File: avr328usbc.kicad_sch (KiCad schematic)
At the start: 18 parts, among them J1 USB-C THT, J2 MCP Debug Header, J3 USB-C THT, U1 MCP2221AxP, U2 ACPL-772L-000E, U3 ACPL-772L-000E

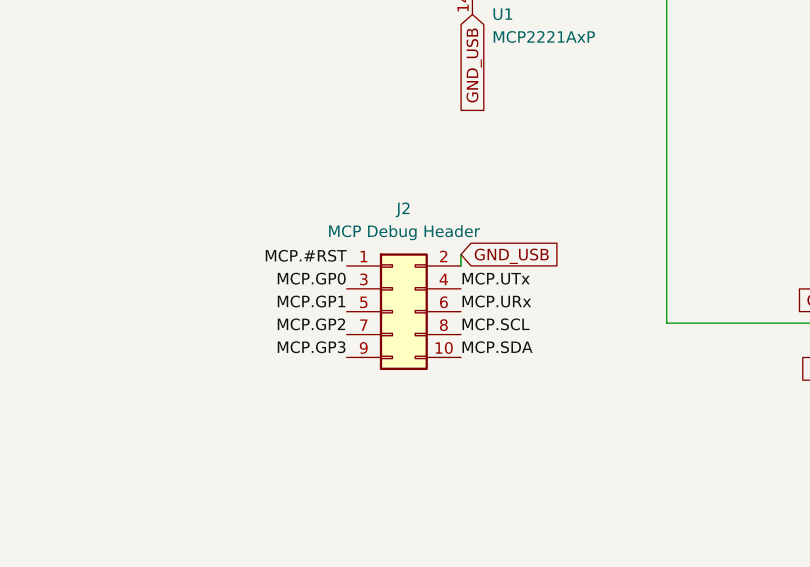
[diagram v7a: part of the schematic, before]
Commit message: reordered pins and routed MCP header
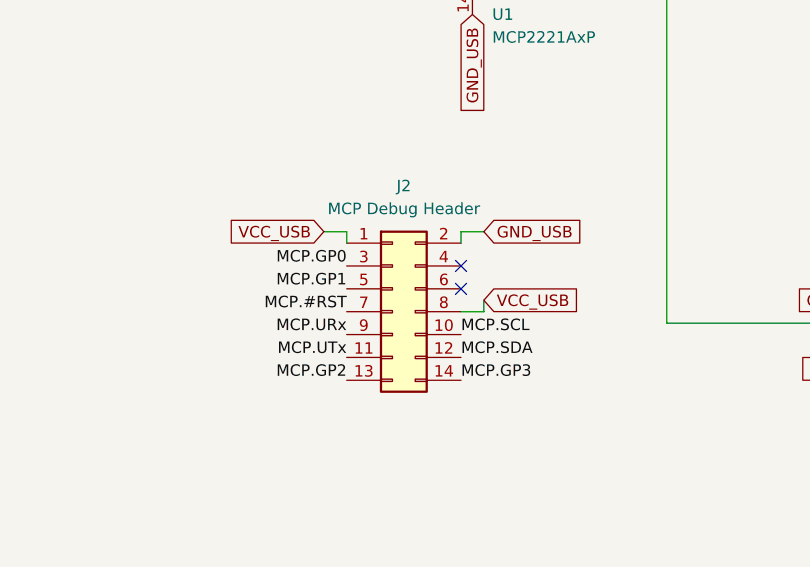
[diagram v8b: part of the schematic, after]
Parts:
- J2: footprint Connector_PinHeader_2.54mm:PinHeader_2x05_P2.54mm_Vertical -> Connector_PinHeader_2.54mm:PinHeader_2x07_P2.54mm_Vertical; symbol Connector_Generic:Conn_02x05_Odd_Even -> Connector_Generic:Conn_02x07_Odd_Even
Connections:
- net MCP.#RST: now also J2.7 (Pin_7); no longer J2.1 (Pin_1)
- net MCP.GP2: now also J2.13 (Pin_13); no longer J2.7 (Pin_7)
- net MCP.GP3: now also J2.14 (Pin_14); no longer J2.9 (Pin_9)
- net MCP.SCL: now also J2.10 (Pin_10); no longer J2.8 (Pin_8)
- net MCP.SDA: now also J2.12 (Pin_12); no longer J2.10 (Pin_10)
- net MCP.URx: now also J2.9 (Pin_9); no longer J2.6 (Pin_6)
- net MCP.UTx: now also J2.11 (Pin_11); no longer J2.4 (Pin_4)
- net VCC_USB: now also J2.1 (Pin_1), J2.8 (Pin_8)
- no-connect marks 8 -> 10
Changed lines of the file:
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@@
+	)
+	(no_connect
+		(at 104.14 118.11)
 	)
 	(no_connect
 		(at 45.72 68.58)
 	)
+	(no_connect
+		(at 104.14 120.65)
+	)
 	(wire
 		(pts
@@
 	(wire
 		(pts
+			(xy 106.68 121.92) (xy 106.68 123.19)
+		)
+		(stroke
+			(width 0)
+			(type default)
+		)
+	)
+	(wire
+		(pts
 			(xy 52.07 74.93) (xy 95.25 74.93)
 		)
@@
 	(wire
 		(pts
+			(xy 104.14 114.3) (xy 104.14 115.57)
+		)
+		(stroke
+			(width 0)
+			(type default)
+		)
+	)
+	(wire
+		(pts
 			(xy 24.13 161.29) (xy 24.13 166.37)
 		)
@@
 	(wire
 		(pts
+			(xy 88.9 114.3) (xy 91.44 114.3)
+		)
+		(stroke
+			(width 0)
+			(type default)
+		)
+	)
+	(wire
+		(pts
 			(xy 64.77 179.07) (xy 52.07 179.07)
 		)
@@
 	(wire
 		(pts
+			(xy 91.44 114.3) (xy 91.44 115.57)
+		)
+		(stroke
+			(width 0)
+			(type default)
+		)
+	)
+	(wire
+		(pts
 			(xy 121.92 179.07) (xy 107.95 179.07)
 		)
@@
 	(wire
 		(pts
+			(xy 106.68 123.19) (xy 104.14 123.19)
+		)
+		(stroke
+			(width 0)
+			(type default)
+		)
+	)
+	(wire
+		(pts
 			(xy 59.69 60.96) (xy 45.72 60.96)
 		)
@@
 	(wire
 		(pts
+			(xy 106.68 114.3) (xy 104.14 114.3)
+		)
+		(stroke
+			(width 0)
+			(type default)
+		)
+	)
+	(wire
+		(pts
 			(xy 198.12 104.14) (xy 198.12 110.49)
 		)
@@
 	(wire
 		(pts
-			(xy 104.14 116.84) (xy 104.14 118.11)
-		)
-		(stroke
-			(width 0)
-			(type default)
-		)
-	)
-	(wire
-		(pts
 			(xy 107.95 57.15) (xy 107.95 34.29)
 		)
@@
 	)
 	(label "MCP.URx"
-		(at 104.14 123.19 0)
-		(fields_autoplaced yes)
-		(effects
-			(font
-				(size 1.27 1.27)
-			)
-			(justify left bottom)
+		(at 91.44 125.73 180)
+		(fields_autoplaced yes)
+		(effects
+			(font
+				(size 1.27 1.27)
+			)
+			(justify right bottom)
 		)
 	)
@@
 	)
 	(label "MCP.GP0"
-		(at 91.44 120.65 180)
+		(at 91.44 118.11 180)
 		(fields_autoplaced yes)
 		(effects
@@
 	)
 	(label "MCP.GP1"
-		(at 91.44 123.19 180)
+		(at 91.44 120.65 180)
 		(fields_autoplaced yes)
 		(effects
@@
 	)
 	(label "MCP.GP3"
-		(at 91.44 128.27 180)
-		(fields_autoplaced yes)
-		(effects
-			(font
-				(size 1.27 1.27)
-			)
-			(justify right bottom)
+		(at 104.14 130.81 0)
+		(fields_autoplaced yes)
+		(effects
+			(font
+				(size 1.27 1.27)
+			)
+			(justify left bottom)
 		)
 	)
@@
 	)
 	(label "MCP.GP2"
-		(at 91.44 125.73 180)
+		(at 91.44 130.81 180)
 		(fields_autoplaced yes)
 		(effects
@@
 	)
 	(label "MCP.UTx"
-		(at 104.14 120.65 0)
-		(fields_autoplaced yes)
-		(effects
-			(font
-				(size 1.27 1.27)
-			)
-			(justify left bottom)
+		(at 91.44 128.27 180)
+		(fields_autoplaced yes)
+		(effects
+			(font
+				(size 1.27 1.27)
+			)
+			(justify right bottom)
 		)
 	)
@@
 	)
 	(label "MCP.#RST"
-		(at 91.44 118.11 180)
+		(at 91.44 123.19 180)
 		(fields_autoplaced yes)
 		(effects
@@
 	(global_label "VCC_USB"
 		(shape input)
+		(at 106.68 121.92 0)
+		(fields_autoplaced yes)
+		(effects
+			(font
+				(size 1.27 1.27)
+			)
+			(justify left)
+		)
+		(property "Intersheetrefs" "${INTERSHEET_REFS}"
+			(at 118.0714 121.92 0)
+			(effects
+				(font
+					(size 1.27 1.27)
+				)
+				(justify left)
+				(hide yes)
+			)
+		)
+	)
+	(global_label "VCC_USB"
+		(shape input)
 		(at 152.4 129.54 180)
 		(fields_autoplaced yes)
@@
 		)
 	)
+	(global_label "VCC_USB"
+		(shape input)
+		(at 88.9 114.3 180)
+		(fields_autoplaced yes)
+		(effects
+			(font
+				(size 1.27 1.27)
+			)
+			(justify right)
+		)
+		(property "Intersheetrefs" "${INTERSHEET_REFS}"
+			(at 77.5086 114.3 0)
+			(effects
+				(font
+					(size 1.27 1.27)
+				)
+				(justify right)
+				(hide yes)
+			)
+		)
+	)
 	(global_label "GND_AVR"
 		(shape input)
@@
 	(global_label "GND_USB"
 		(shape input)
-		(at 104.14 116.84 0)
+		(at 106.68 114.3 0)
 		(fields_autoplaced yes)
 		(effects
@@
 		)
 		(property "Intersheetrefs" "${INTERSHEET_REFS}"
-			(at 115.7733 116.84 0)
+			(at 118.3133 114.3 0)
 			(effects
 				(font
@@
 	)
 	(symbol
-		(lib_id "Connector_Generic:Conn_02x05_Odd_Even")
+		(lib_id "Connector_Generic:Conn_02x07_Odd_Even")
 		(at 96.52 123.19 0)
 		(unit 1)
@@
 		(fields_autoplaced yes)
 		(property "Reference" "J2"
+			(at 97.79 109.22 0)
+			(effects
+				(font
+					(size 1.27 1.27)
+				)
+			)
+		)
+		(property "Value" "MCP Debug Header"
 			(at 97.79 111.76 0)
 			(effects
@@
 			)
 		)
-		(property "Value" "MCP Debug Header"
-			(at 97.79 114.3 0)
-			(effects
-				(font
-					(size 1.27 1.27)
-				)
-			)
-		)
-		(property "Footprint" "Connector_PinHeader_2.54mm:PinHeader_2x05_P2.54mm_Vertical"
+		(property "Footprint" "Connector_PinHeader_2.54mm:PinHeader_2x07_P2.54mm_Vertical"
 			(at 96.52 123.19 0)
 			(effects
@@
 			)
 		)
-		(property "Description" "Generic connector, double row, 02x05, odd/even pin numbering scheme (row 1 odd numbers, row 2 even numbers), script generated (kicad-library-utils/schlib/autogen/connector/)"
+		(property "Description" "Generic connector, double row, 02x07, odd/even pin numbering scheme (row 1 odd numbers, row 2 even numbers), script generated (kicad-library-utils/schlib/autogen/connector/)"
 			(at 96.52 123.19 0)
 			(effects
@@
 		(pin "2"
 		)
+		(pin "12"
+		)
+		(pin "11"
+		)
+		(pin "14"
+		)
+		(pin "13"
+		)
 		(instances
